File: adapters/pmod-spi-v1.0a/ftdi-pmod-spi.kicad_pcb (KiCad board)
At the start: 2 copper layers, 16 x 18 mm, 2 parts, among them J1 Conn, J4 Prog

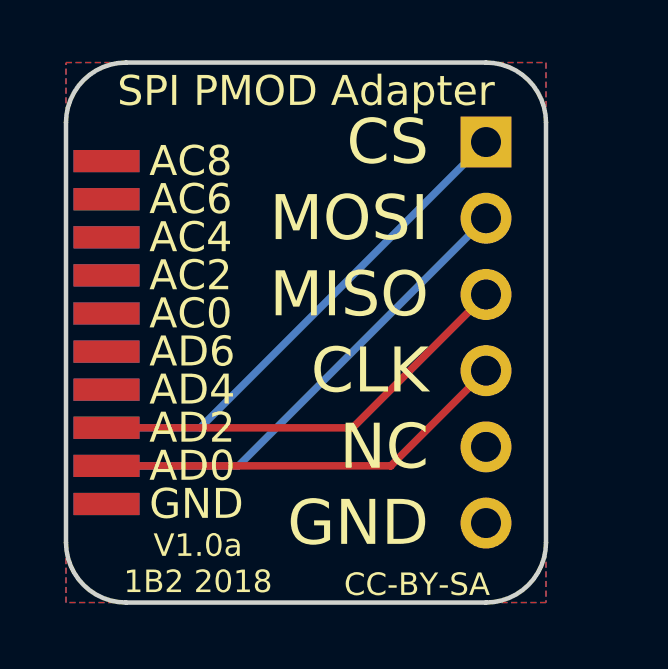
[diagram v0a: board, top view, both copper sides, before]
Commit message: Updated the SPI PMOD adapter to a full PMOD interface.
This setup allows the use of the adapter with INT and RST lines too.
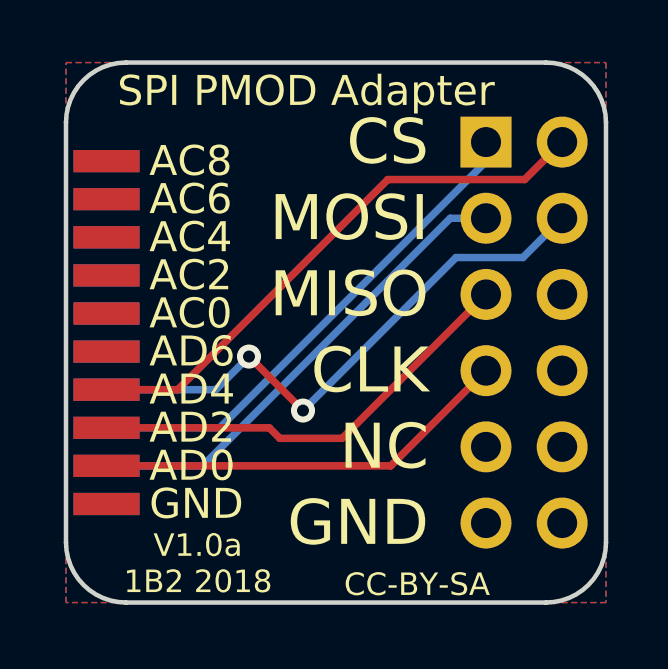
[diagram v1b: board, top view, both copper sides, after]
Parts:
- J4: footprint Connector_PinSocket_2.54mm:PinSocket_1x06_P2.54mm_Vertical -> Connector_PinSocket_2.54mm:PinSocket_2x06_P2.54mm_Horizontal
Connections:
- J4 pad 2: /DO -> /GPIOL0
- J4 pad 3: /DI -> /DO
- J4 pad 4: /SK -> /GPIOL1
- J4 pad 5: Net-(J4-Pad5) -> /DI
- J4 pad 6: GND -> Net-(J4-Pad6)
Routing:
- net /GPIOL1: track 0.00 -> 19.0 mm, vias 0 -> 2
- net /GPIOL0: track 0.00 -> 18.6 mm
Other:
- board size 16 x 18 mm -> 18 x 18 mm

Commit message: Fixed PMOD pinout on SPI adapter.
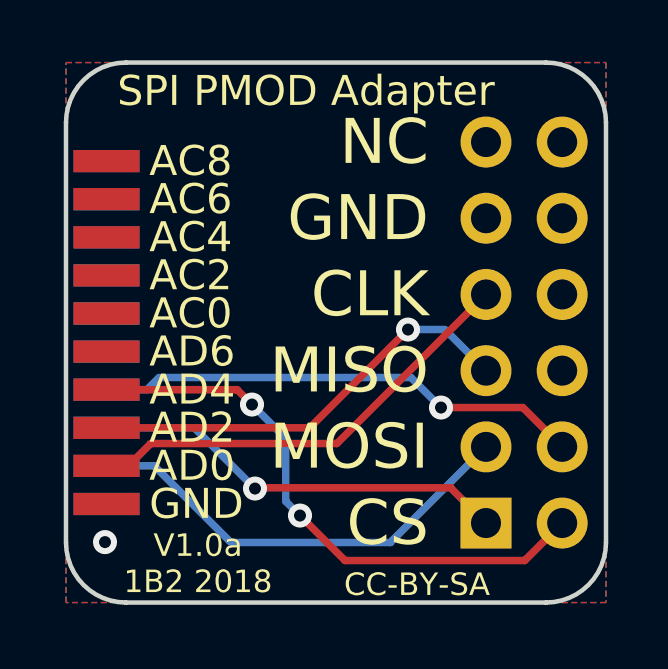
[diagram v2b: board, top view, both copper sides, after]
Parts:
- J4: value Prog -> PMOD; footprint Connector_PinSocket_2.54mm:PinSocket_2x06_P2.54mm_Horizontal -> Connector_PinHeader_2.54mm:PinHeader_2x06_P2.54mm_Horizontal
- moved J4 12.7 mm to (44.0, 50.4), turned to 0 degrees
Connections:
- J4 pad 10: Net-(J4-Pad10) -> GND
- J4 pad 11: GND -> Net-(J4-Pad11)
- J4 pad 12: GND -> Net-(J4-Pad12)
- J4 pad 9: Net-(J4-Pad9) -> GND
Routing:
- net /CS: track 17.0 -> 14.0 mm, vias 0 -> 1
- net /GPIOL1: track 19.0 -> 16.3 mm, vias 2 -> 1
- net /SK: track 14.0 -> 15.0 mm
- net /DO: track 16.1 -> 15.0 mm
- net /GPIOL0: track 18.6 -> 19.3 mm, vias 0 -> 2
- net /DI: track 14.8 -> 14.6 mm, vias 0 -> 1
- net GND: vias 0 -> 1
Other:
- rule pad_to_mask_clearance: 0.2 -> 0.05
